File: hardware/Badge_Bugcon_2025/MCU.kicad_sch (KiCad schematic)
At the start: 64 parts, among them J1 Flash, J11 +3V3, J12 CODEC, J13 ETH, J14 +1V8, J2 Conn_01x04, J5 +3V3, SW2 SW_Push, SW3 SW_Push, U6 W25N02KVZEIR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

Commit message: feat(Hw):Update_Schematic
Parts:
- removed J11: +3V3, Connector_PinHeader_2.54mm:PinHeader_1x21_P2.54mm_Vertical, symbol Connector_Generic:Conn_01x21
- removed J5: +3V3, Connector_PinHeader_2.54mm:PinHeader_1x22_P2.54mm_Vertical, symbol Connector_Generic:Conn_01x22
- added J5: 3V3, symbol Connector_Generic:Conn_01x24
- added J8: 3V3, symbol Connector_Generic:Conn_01x23
- R2: LCSC# (none) -> C25094
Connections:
- net +3V3: now also J5.1 (Pin_1), J8.1 (Pin_1)
- net GND: now also J5.24 (Pin_24), J8.23 (Pin_23)
- net GPIO0_A2_D: now also J5.14 (Pin_14)
- net GPIO0_A5_D: now also J5.17 (Pin_17)
- net GPIO0_A6_D: now also J5.18 (Pin_18)
- net GPIO1_A2_D: now also J5.19 (Pin_19)
- net GPIO1_A3_D: now also J5.20 (Pin_20)
- net GPIO1_A4_D: now also J5.21 (Pin_21)
- net GPIO1_B0_D: now also J5.22 (Pin_22)
- net GPIO1_B1_D: now also J5.23 (Pin_23)
- net GPIO1_C0_D: now also J8.12 (Pin_12)
- net GPIO1_C1_D: now also J8.11 (Pin_11)
- net GPIO1_C3_D: now also J8.10 (Pin_10)
- net GPIO1_C4_D: now also J8.9 (Pin_9)
- net GPIO1_C5_D: now also J8.8 (Pin_8)
- net GPIO1_C6_D: now also J8.2 (Pin_2)
- net GPIO1_C7_D: now also J8.3 (Pin_3)
- net GPIO1_D0_D: now also J8.7 (Pin_7)
- net GPIO1_D1_D: now also J8.6 (Pin_6)
- net GPIO1_D2_D: now also J8.5 (Pin_5)
- net GPIO1_D3_D: now also J8.4 (Pin_4)
- net GPIO2_A0_D_1: now also J8.17 (Pin_17)
- net GPIO2_A0_D_2: now also J8.18 (Pin_18)
- net GPIO2_A3_D: now also J8.20 (Pin_20)
- net GPIO2_A4_D: now also J8.21 (Pin_21)
- net GPIO2_A5_D: now also J8.22 (Pin_22)
- net GPIO2_A6_D: now also J8.16 (Pin_16)
- net GPIO2_A7_D: now also J8.15 (Pin_15)
- net GPIO2_A_2_D: now also J8.19 (Pin_19)
- net GPIO2_B1_D_1: now also J8.13 (Pin_13)
- net GPIO2_B1_D_2: now also J8.14 (Pin_14)
- net GPIO3_A2_U: now also J5.2 (Pin_2)
- net GPIO3_A3_U: now also J5.3 (Pin_3)
- net GPIO3_A4_D: now also J5.4 (Pin_4)
- net GPIO3_A5_U: now also J5.5 (Pin_5)
- net GPIO3_A6_U: now also J5.6 (Pin_6)
- net GPIO3_A7_U: now also J5.7 (Pin_7)
- net GPIO4_A0_U: now also J5.11 (Pin_11)
- net GPIO4_A1_U: now also J5.10 (Pin_10)
- net GPIO4_A5_U: now also J5.9 (Pin_9)
- net GPIO4_A7_U: now also J5.8 (Pin_8)
- net DOWN renamed GPIO0_A3_U
- net GPIO0_A3_U: now also J5.15 (Pin_15)
- net LEFT renamed GPIO0_A0_Z
- net GPIO0_A0_Z: now also J5.12 (Pin_12)
- net RIGHT renamed GPIO0_A1_D
- net GPIO0_A1_D: now also J5.13 (Pin_13)
- net UP renamed GPIO0_A4_D
- net GPIO0_A4_D: now also J5.16 (Pin_16)

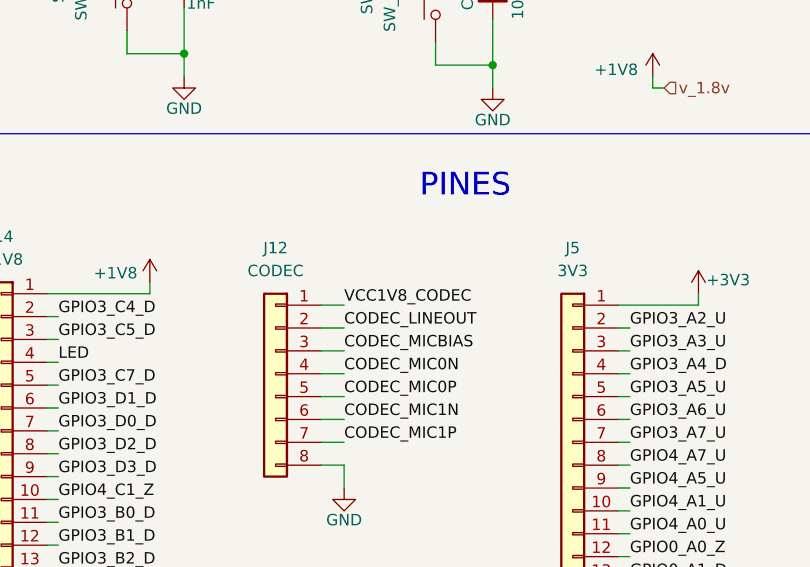
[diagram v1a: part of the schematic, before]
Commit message: feat(Hw):Update_Schematic_And_Floorplan
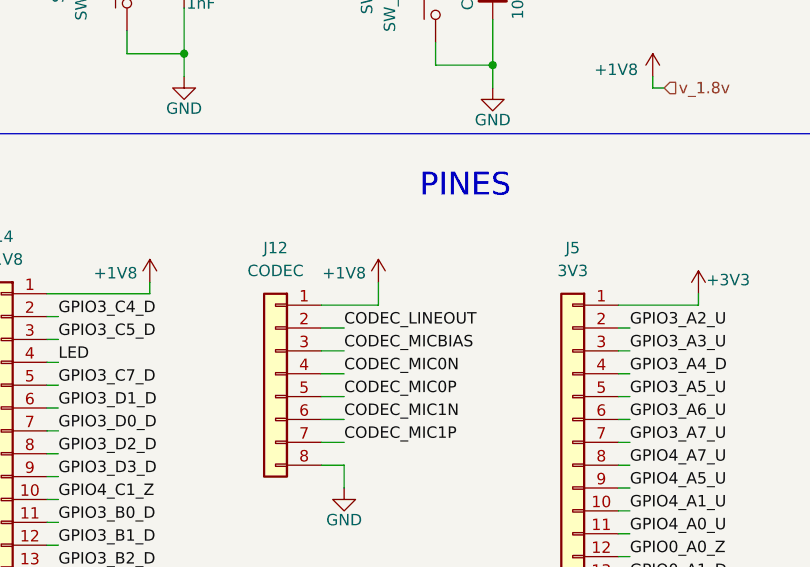
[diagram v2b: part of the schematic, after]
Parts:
- J5: footprint (none) -> Connector_PinSocket_2.54mm:PinSocket_1x24_P2.54mm_Vertical
- J8: footprint (none) -> Connector_PinSocket_2.54mm:PinSocket_1x23_P2.54mm_Vertical
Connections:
- net +1V8: now also J12.1 (Pin_1)
- net VCC1V8_CODEC: no longer J12.1 (Pin_1)
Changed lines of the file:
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@@
 	(wire
 		(pts
+			(xy 59.69 217.17) (xy 53.34 217.17)
+		)
+		(stroke
+			(width 0)
+			(type default)
+		)
+	)
+	(wire
+		(pts
 			(xy 38.1 171.45) (xy 43.18 171.45)
 		)
@@
 	(wire
 		(pts
+			(xy 59.69 217.17) (xy 59.69 214.63)
+		)
+		(stroke
+			(width 0)
+			(type default)
+		)
+	)
+	(wire
+		(pts
 			(xy 24.13 236.22) (xy 22.86 236.22)
 		)
@@
 	(wire
 		(pts
-			(xy 55.88 217.17) (xy 53.34 217.17)
-		)
-		(stroke
-			(width 0)
-			(type default)
-		)
-	)
-	(wire
-		(pts
 			(xy 87.63 260.35) (xy 86.36 260.35)
 		)
@@
 		)
 	)
-	(label "VCC1V8_CODEC"
-		(at 55.88 217.17 0)
-		(effects
-			(font
-				(size 1.27 1.27)
-			)
-			(justify left bottom)
-		)
-	)
 	(label "ETH_PHY_RXP"
 		(at 55.88 261.62 0)
@@
 	)
 	(symbol
+		(lib_id "power:+1V8")
+		(at 59.69 214.63 0)
+		(mirror y)
+		(unit 1)
+		(exclude_from_sim no)
+		(in_bom yes)
+		(on_board yes)
+		(dnp no)
+		(property "Reference" "#PWR09"
+			(at 59.69 218.44 0)
+			(effects
+				(font
+					(size 1.27 1.27)
+				)
+				(hide yes)
+			)
+		)
+		(property "Value" "+1V8"
+			(at 55.88 213.614 0)
+			(effects
+				(font
+					(size 1.27 1.27)
+				)
+			)
+		)
+		(property "Footprint" ""
+			(at 59.69 214.63 0)
+			(effects
+				(font
+					(size 1.27 1.27)
+				)
+				(hide yes)
+			)
+		)
+		(property "Datasheet" ""
+			(at 59.69 214.63 0)
+			(effects
+				(font
+					(size 1.27 1.27)
+				)
+				(hide yes)
+			)
+		)
+		(property "Description" "Power symbol creates a global label with name \"+1V8\""
+			(at 59.69 214.63 0)
+			(effects
+				(font
+					(size 1.27 1.27)
+				)
+				(hide yes)
+			)
+		)
+		(pin "1"
+		)
+		(instances
+			(project "Badge_Bugcon_2025"
+				(path "/a95785a0-0aa1-454e-b59f-0ac64970ac71/b4a4bbe3-3d97-4ef8-9067-81f34711c2c0"
+					(reference "#PWR09")
+					(unit 1)
+				)
+			)
+		)
+	)
+	(symbol
 		(lib_id "Device:C_Small")
 		(at 74.93 140.97 0)
@@
 			)
 		)
-		(property "Footprint" ""
+		(property "Footprint" "Connector_PinSocket_2.54mm:PinSocket_1x24_P2.54mm_Vertical"
 			(at 81.28 245.11 0)
 			(effects
@@
 			)
 		)
-		(property "Footprint" ""
+		(property "Footprint" "Connector_PinSocket_2.54mm:PinSocket_1x23_P2.54mm_Vertical"
 			(at 111.76 246.38 0)
 			(effects

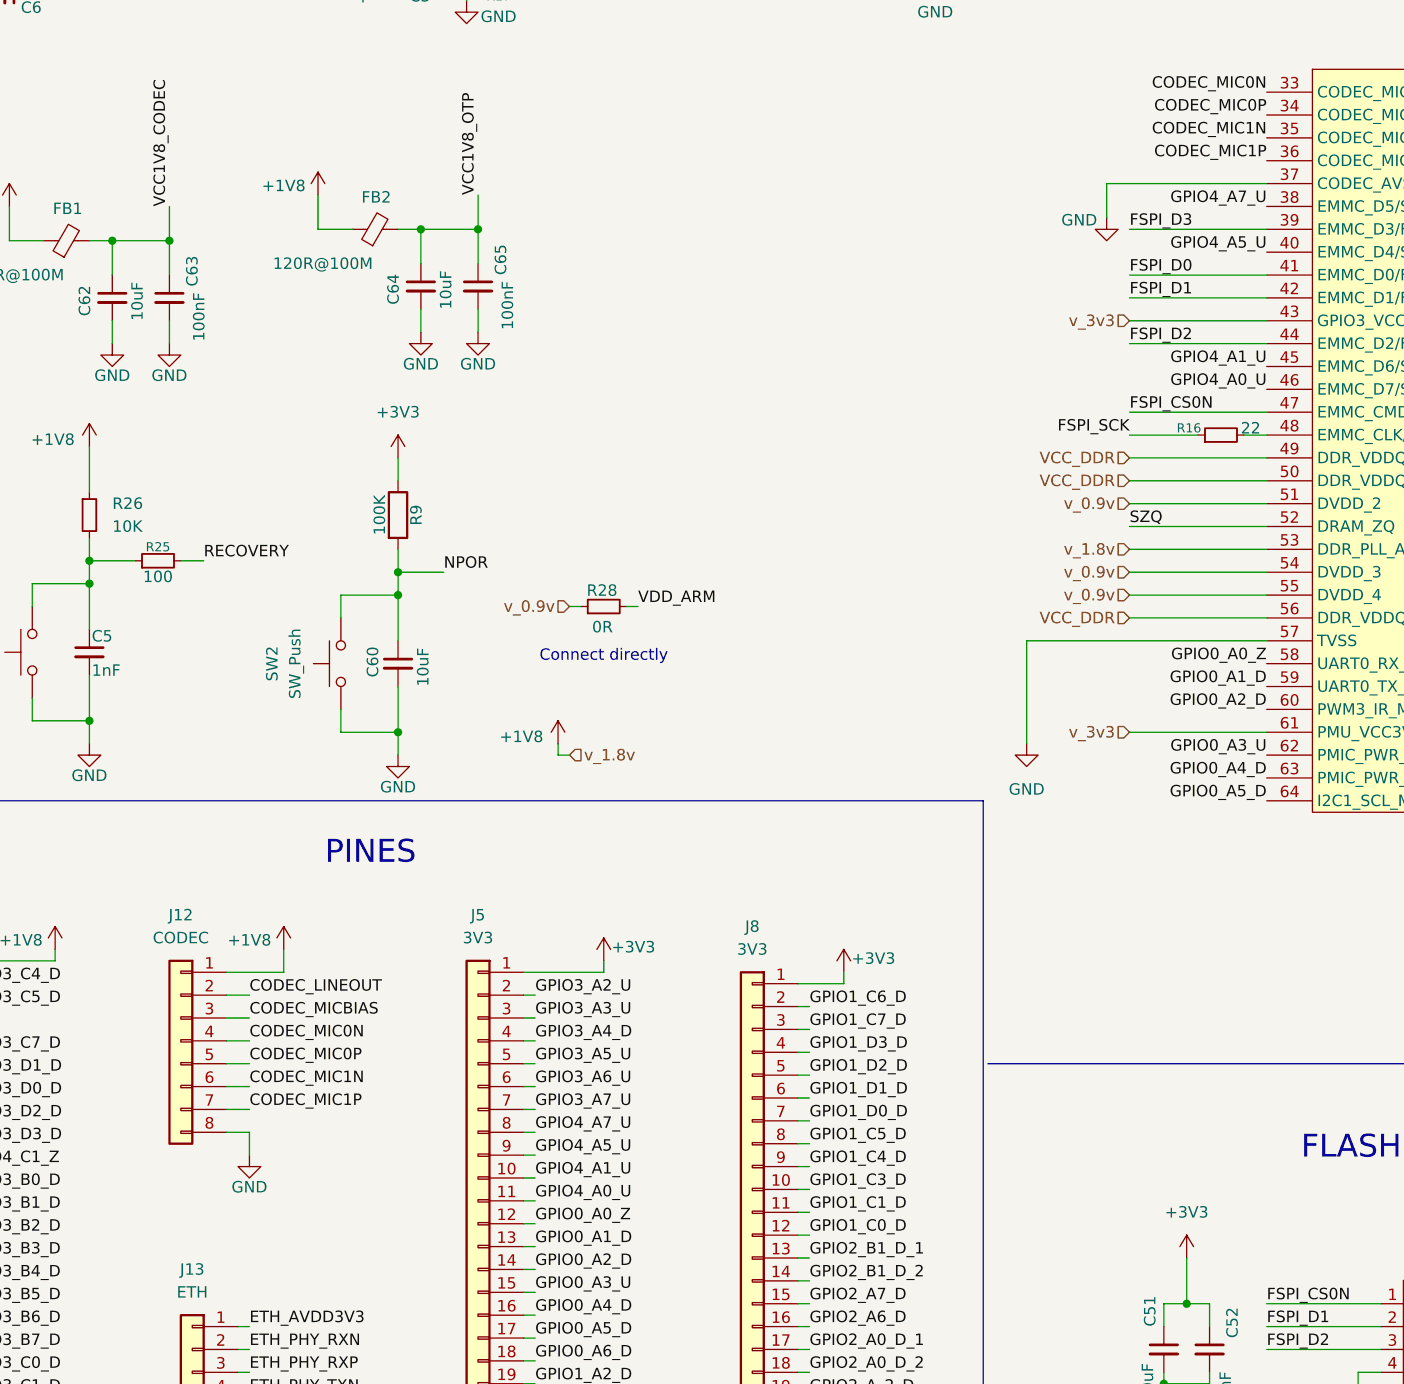
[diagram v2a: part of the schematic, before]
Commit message: feat(Hw):Update_Schematic_And_Floorplan
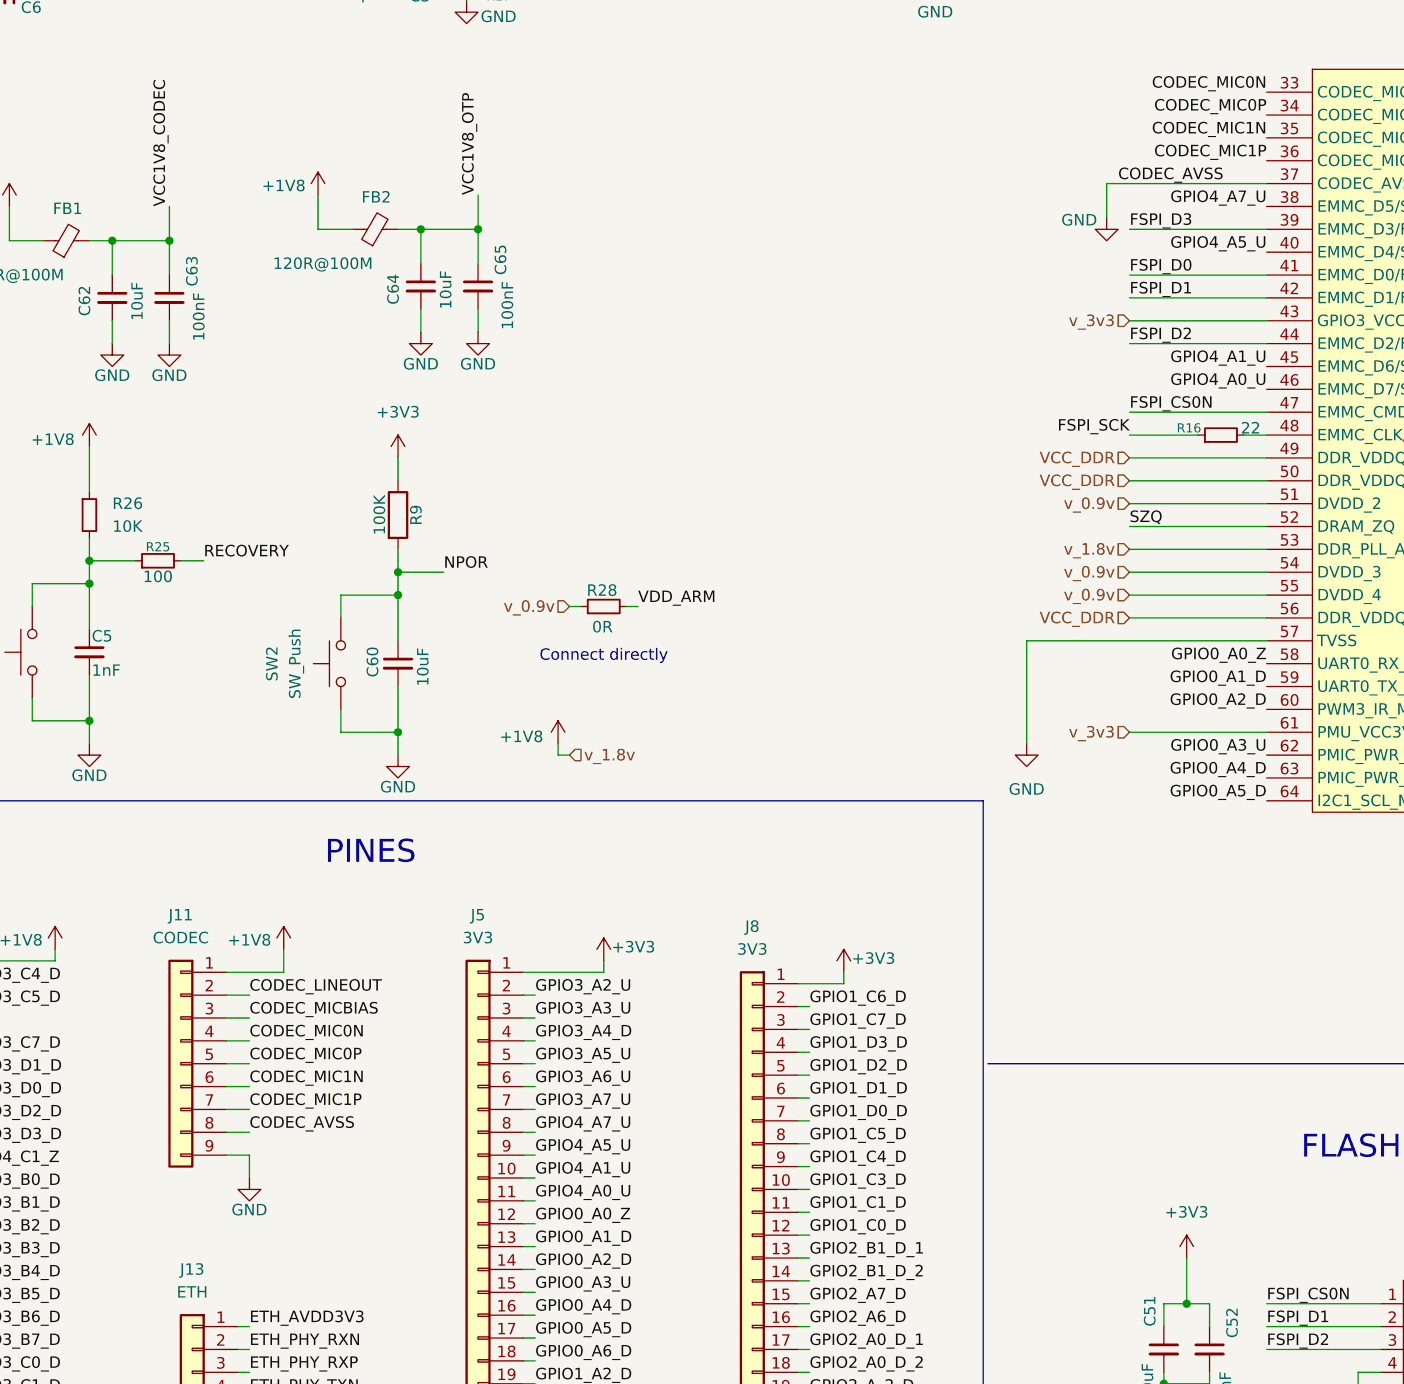
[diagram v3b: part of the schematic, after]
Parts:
- removed J12: CODEC, Connector_PinHeader_2.54mm:PinHeader_1x08_P2.54mm_Vertical, symbol Connector_Generic:Conn_01x08
- added J11: CODEC, symbol Connector_Generic:Conn_01x09
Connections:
- net +1V8: now also J11.1 (Pin_1)
- net CODEC_LINEOUT: now also J11.2 (Pin_2)
- net CODEC_MIC0N: now also J11.4 (Pin_4)
- net CODEC_MIC0P: now also J11.5 (Pin_5)
- net CODEC_MIC1N: now also J11.6 (Pin_6)
- net CODEC_MIC1P: now also J11.7 (Pin_7)
- net CODEC_MICBIAS: now also J11.3 (Pin_3)
- net GND: now also J11.8 (Pin_8), J11.9 (Pin_9)
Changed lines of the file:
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@@
 	(wire
 		(pts
-			(xy 55.88 237.49) (xy 55.88 234.95)
+			(xy 55.88 240.03) (xy 55.88 237.49)
 		)
 		(stroke
@@
 	(wire
 		(pts
-			(xy 55.88 234.95) (xy 53.34 234.95)
+			(xy 55.88 237.49) (xy 53.34 237.49)
 		)
 		(stroke
@@
 	(wire
 		(pts
+			(xy 55.88 234.95) (xy 53.34 234.95)
+		)
+		(stroke
+			(width 0)
+			(type default)
+		)
+	)
+	(wire
+		(pts
 			(xy 91.44 34.29) (xy 91.44 36.83)
 		)
@@
 		)
 	)
+	(label "CODEC_AVSS"
+		(at 152.4 129.54 0)
+		(effects
+			(font
+				(size 1.27 1.27)
+			)
+			(justify left bottom)
+		)
+	)
 	(label "GPIO2_A_2_D"
 		(at 289.56 156.21 180)
@@
 		)
 	)
+	(label "CODEC_AVSS"
+		(at 55.88 234.95 0)
+		(effects
+			(font
+				(size 1.27 1.27)
+			)
+			(justify left bottom)
+		)
+	)
 	(label "GPIO2_B1_D_2"
 		(at 289.56 140.97 180)
@@
 	)
 	(symbol
-		(lib_id "Connector_Generic:Conn_01x08")
-		(at 48.26 224.79 0)
-		(mirror y)
-		(unit 1)
-		(exclude_from_sim no)
-		(in_bom yes)
-		(on_board yes)
-		(dnp no)
-		(fields_autoplaced yes)
-		(property "Reference" "J12"
-			(at 48.26 210.82 0)
-			(effects
-				(font
-					(size 1.27 1.27)
-				)
-			)
-		)
-		(property "Value" "CODEC"
-			(at 48.26 213.36 0)
-			(effects
-				(font
-					(size 1.27 1.27)
-				)
-			)
-		)
-		(property "Footprint" "Connector_PinHeader_2.54mm:PinHeader_1x08_P2.54mm_Vertical"
-			(at 48.26 224.79 0)
-			(effects
-				(font
-					(size 1.27 1.27)
-				)
-				(hide yes)
-			)
-		)
-		(property "Datasheet" "~"
-			(at 48.26 224.79 0)
-			(effects
-				(font
-					(size 1.27 1.27)
-				)
-				(hide yes)
-			)
-		)
-		(property "Description" "Generic connector, single row, 01x08, script generated (kicad-library-utils/schlib/autogen/connector/)"
-			(at 48.26 224.79 0)
-			(effects
-				(font
-					(size 1.27 1.27)
-				)
-				(hide yes)
-			)
-		)
-		(property "manf#" ""
-			(at 48.26 224.79 0)
-			(effects
-				(font
-					(size 1.27 1.27)
-				)
-				(hide yes)
-			)
-		)
-		(property "Availability" ""
-			(at 48.26 224.79 0)
-			(effects
-				(font
-					(size 1.27 1.27)
-				)
-				(hide yes)
-			)
-		)
-		(property "Check_prices" ""
-			(at 48.26 224.79 0)
-			(effects
-				(font
-					(size 1.27 1.27)
-				)
-				(hide yes)
-			)
-		)
-		(property "Description_1" ""
-			(at 48.26 224.79 0)
-			(effects
-				(font
-					(size 1.27 1.27)
-				)
-				(hide yes)
-			)
-		)
-		(property "MANUFACTURER" ""
-			(at 48.26 224.79 0)
-			(effects
-				(font
-					(size 1.27 1.27)
-				)
-				(hide yes)
-			)
-		)
-		(property "MAXIMUM_PACKAGE_HEIGHT" ""
-			(at 48.26 224.79 0)
-			(effects
-				(font
-					(size 1.27 1.27)
-				)
-				(hide yes)
-			)
-		)
-		(property "MF" ""
-			(at 48.26 224.79 0)
-			(effects
-				(font
-					(size 1.27 1.27)
-				)
-				(hide yes)
-			)
-		)
-		(property "MP" ""
-			(at 48.26 224.79 0)
-			(effects
-				(font
-					(size 1.27 1.27)
-				)
-				(hide yes)
-			)
-		)
-		(property "PARTREV" ""
-			(at 48.26 224.79 0)
-			(effects
-				(font
-					(size 1.27 1.27)
-				)
-				(hide yes)
-			)
-		)
-		(property "Package" ""
-			(at 48.26 224.79 0)
-			(effects
-				(font
-					(size 1.27 1.27)
-				)
-				(hide yes)
-			)
-		)
-		(property "Price" ""
-			(at 48.26 224.79 0)
-			(effects
-				(font
-					(size 1.27 1.27)
-				)
-				(hide yes)
-			)
-		)
-		(property "STANDARD" ""
-			(at 48.26 224.79 0)
-			(effects
-				(font
-					(size 1.27 1.27)
-				)
-				(hide yes)
-			)
-		)
-		(property "SnapEDA_Link" ""
-			(at 48.26 224.79 0)
-			(effects
-				(font
-					(size 1.27 1.27)
-				)
-				(hide yes)
-			)
-		)
-		(pin "3"
-		)
-		(pin "6"
-		)
-		(pin "4"
-		)
-		(pin "8"
-		)
-		(pin "2"
-		)
-		(pin "7"
-		)
-		(pin "5"
-		)
-		(pin "1"
-		)
-		(instances
-			(project ""
-				(path "/a95785a0-0aa1-454e-b59f-0ac64970ac71/b4a4bbe3-3d97-4ef8-9067-81f34711c2c0"
-					(reference "J12")
-					(unit 1)
-				)
-			)
-		)
-	)
-	(symbol
 		(lib_id "Memory_Flash:W25Q128JVE")
 		(at 196.85 261.62 0)
@@
 	(symbol
 		(lib_id "power:GND")
-		(at 55.88 237.49 0)
+		(at 55.88 240.03 0)
 		(unit 1)
 		(exclude_from_sim no)
@@
 		(dnp no)
 		(property "Reference" "#PWR0167"
-			(at 55.88 243.84 0)
+			(at 55.88 246.38 0)
 			(effects
 				(font
@@
 		)
 		(property "Value" "GND"
-			(at 55.88 241.046 0)
+			(at 55.88 243.586 0)
 			(effects
 				(font
@@
 		)
 		(property "Footprint" ""
-			(at 55.88 237.49 0)
+			(at 55.88 240.03 0)
 			(effects
 				(font
@@
 		)
 		(property "Datasheet" ""
-			(at 55.88 237.49 0)
+			(at 55.88 240.03 0)
 			(effects
 				(font
@@
 		)
 		(property "Description" "Power symbol creates a global label with name \"GND\" , ground"
-			(at 55.88 237.49 0)
+			(at 55.88 240.03 0)
 			(effects
 				(font
@@
 					(unit 1)
 				)
+			)
+		)
+	)
+	(symbol
+		(lib_id "Connector_Generic:Conn_01x09")
+		(at 48.26 227.33 0)
+		(mirror y)
+		(unit 1)
+		(exclude_from_sim no)
+		(in_bom yes)
+		(on_board yes)
+		(dnp no)
+		(fields_autoplaced yes)
+		(property "Reference" "J11"
+			(at 48.26 210.82 0)
+			(effects
+				(font
+					(size 1.27 1.27)
+				)
+			)
+		)
+		(property "Value" "CODEC"
+			(at 48.26 213.36 0)
+			(effects
+				(font
+					(size 1.27 1.27)
+				)
+			)
+		)
+		(property "Footprint" ""
+			(at 48.26 227.33 0)
+			(effects
+				(font
+					(size 1.27 1.27)
+				)
+				(hide yes)
+			)
+		)
+		(property "Datasheet" "~"
+			(at 48.26 227.33 0)
+			(effects
+				(font
+					(size 1.27 1.27)
+				)
+				(hide yes)
+			)
+		)
+		(property "Description" "Generic connector, single row, 01x09, script generated (kicad-library-utils/schlib/autogen/connector/)"
+			(at 48.26 227.33 0)
+			(effects
+				(font
+					(size 1.27 1.27)
+				)
+				(hide yes)
+			)
+		)
+		(pin "5"
+		)
+		(pin "1"
+		)
+		(pin "7"
+		)
+		(pin "8"
+		)
+		(pin "6"
+		)
+		(pin "9"
+		)
+		(pin "3"
+		)
+		(pin "4"
+		)
+		(pin "2"
+		)
+		(instances
+			(project ""
+				(path "/a95785a0-0aa1-454e-b59f-0ac64970ac71/b4a4bbe3-3d97-4ef8-9067-81f34711c2c0"
+					(reference "J11")
+					(unit 1)
+				)
